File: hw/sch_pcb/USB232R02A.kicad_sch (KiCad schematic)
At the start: 36 parts, among them J1 USB_B, J10 HEADER_2x01_PARALLEL, J11 HEADER_2x01_PARALLEL, J12 HEADER_2x01_PARALLEL, J13 HEADER_2x01_PARALLEL, J14 HEADER_2x01_PARALLEL, J15 HEADER_2x01_PARALLEL, J16 HEADER_2x01_PARALLEL, J2 HEADER_2x03_PARALLEL, J3 HEADER_2x03_PARALLEL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

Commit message: Edit
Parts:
- removed J13, J14, J15, J16: HEADER_2x01_PARALLEL, Mlab_Pin_Headers:Straight_2x01, symbol MLAB_HEADER:HEADER_2x01_PARALLEL
- added F1: 750mA, Mlab_F:1812, symbol Device:Polyfuse
- added J13, J14, J15, J16: -, Mlab_Pin_Headers:Straight_1x01, symbol MLAB_HEADER:HEADER_1x01
- added J17: HEADER_2x01_PARALLEL, Mlab_Pin_Headers:Straight_2x01, symbol MLAB_HEADER:HEADER_2x01_PARALLEL
- H1, H2, H3, H4: footprint Mlab_Mechanical:dira_3mm -> Mlab_Mechanical:MountingHole_3mm
- J10, J11, J12, J4, J9: value HEADER_2x01_PARALLEL -> -
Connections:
- net CBUS0: now also J13.1
- net CBUS3: now also J16.1
- net D+: now also U1.4 (I/O2); no longer U1.6 (I/O1)
- net D-: now also U1.6 (I/O1); no longer U1.4 (I/O2)
- net DM: now also U1.1 (I/O1); no longer U1.3 (I/O2)
- net DP: now also U1.3 (I/O2); no longer U1.1 (I/O1)
- net GND: now also J17.1, J17.2
- net RXLED/CBUS1: now also J14.1
- net TXLED/CBUS2: now also J15.1
- net VBUS: now also F1.1; no longer C1.1, FB1.1
- new net: C1.1, F1.2, FB1.1

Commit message: Add MLAB title block. Minor layout cleanup Cleanup silkscreen.
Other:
- company: (none) -> jacho
- title: (none) -> USB232R02A

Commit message: Edit
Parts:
- C1: UST_ID (none) -> 5c70984712875079b91f8b49
- C2: UST_ID (none) -> 5c70984812875079b91f8bbd
- C3, C4, C5: UST_ID (none) -> 5c70984712875079b91f8b4c
- D1: UST_ID (none) -> 5c70984512875079b91f88ac
- D2: UST_ID (none) -> 5c70984412875079b91f8896
- D3: UST_ID (none) -> 5c70984412875079b91f8895
- F1: UST_ID (none) -> 5c70984512875079b91f88d2
- J1: UST_ID (none) -> 5c70984412875079b91f87a8
- R1: UST_ID (none) -> 5c70984612875079b91f8995
- R2: UST_ID (none) -> 5c70984612875079b91f899f
- R3, R4: UST_ID (none) -> 5c70984512875079b91f8983
- U1: UST_ID (none) -> 5e82e0691287502a334a778c
- U2: UST_ID (none) -> 605d7fe0128750769e769adb

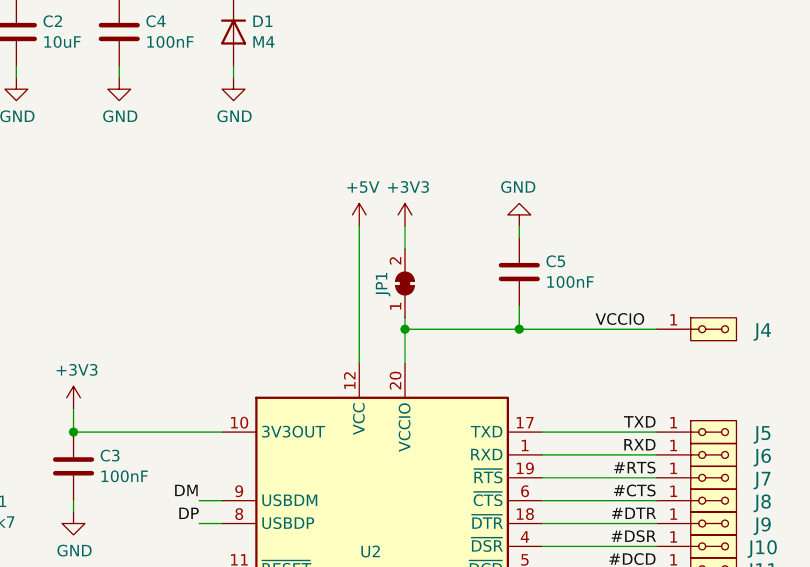
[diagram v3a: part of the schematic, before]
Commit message: vyreseni DRC, uprava sablon
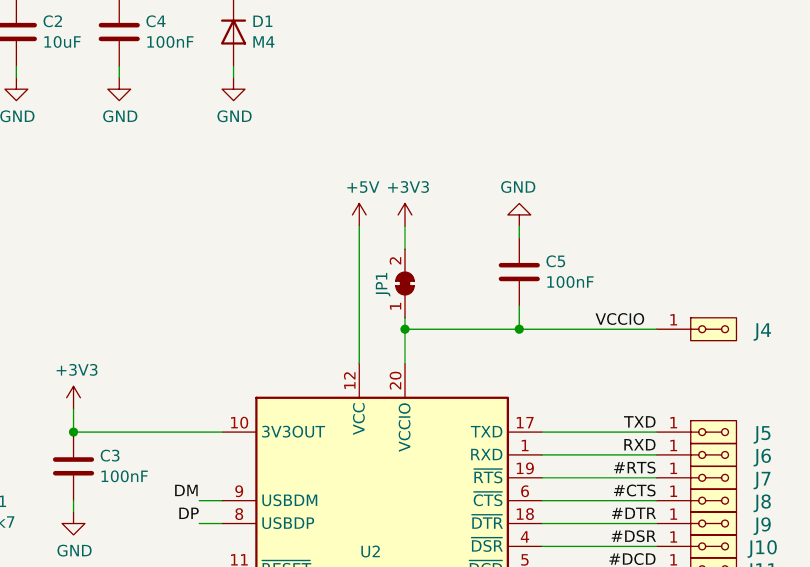
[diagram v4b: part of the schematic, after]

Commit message: Update title block and resolve ERC issues.
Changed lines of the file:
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@@
     (date "2021-03-25")
     (company "jacho")
+    (comment 1 "USB to UART converter")
   )
   (junction (at 54.61 30.48) (diameter 1.016) (color 0 0 0 0)
@@
     (stroke (width 0) (type solid) (color 0 0 0 0))
   )
+  (wire (pts (xy 152.4 93.98) (xy 152.4 95.25))
+    (stroke (width 0) (type default) (color 0 0 0 0))
+  )
   (wire (pts (xy 96.52 55.88) (xy 96.52 57.15))
     (stroke (width 0) (type solid) (color 0 0 0 0))
@@
   (wire (pts (xy 91.44 55.88) (xy 91.44 110.49))
     (stroke (width 0) (type solid) (color 0 0 0 0))
+  )
+  (wire (pts (xy 120.65 55.88) (xy 125.095 55.88))
+    (stroke (width 0) (type default) (color 0 0 0 0))
   )
   (wire (pts (xy 77.47 64.77) (xy 77.47 66.04))
@@
   (label "D+" (at 41.91 27.94 180)
     (effects (font (size 1.27 1.27)) (justify right bottom))
+  )
+  (symbol (lib_id "power:PWR_FLAG") (at 152.4 95.25 180) (unit 1)
+    (in_bom yes) (on_board yes) (fields_autoplaced)
+    (property "Reference" "#FLG0102" (id 0) (at 152.4 97.155 0)
+      (effects (font (size 1.27 1.27)) hide)
+    )
+    (property "Value" "PWR_FLAG" (id 1) (at 152.4 99.6934 0))
+    (property "Footprint" "" (id 2) (at 152.4 95.25 0)
+      (effects (font (size 1.27 1.27)) hide)
+    )
+    (property "Datasheet" "~" (id 3) (at 152.4 95.25 0)
+      (effects (font (size 1.27 1.27)) hide)
+    )
+    (pin "1")
   )
   (symbol (lib_id "Device:LED") (at 226.06 133.35 90) (unit 1)
@@
     (pin "1")
   )
+  (symbol (lib_id "power:PWR_FLAG") (at 125.095 55.88 270) (unit 1)
+    (in_bom yes) (on_board yes) (fields_autoplaced)
+    (property "Reference" "#FLG0101" (id 0) (at 127 55.88 0)
+      (effects (font (size 1.27 1.27)) hide)
+    )
+    (property "Value" "PWR_FLAG" (id 1) (at 128.27 56.3138 90)
+      (effects (font (size 1.27 1.27)) (justify left))
+    )
+    (property "Footprint" "" (id 2) (at 125.095 55.88 0)
+      (effects (font (size 1.27 1.27)) hide)
+    )
+    (property "Datasheet" "~" (id 3) (at 125.095 55.88 0)
+      (effects (font (size 1.27 1.27)) hide)
+    )
+    (pin "1")
+  )
   (symbol (lib_id "Device:R") (at 91.44 127 0) (unit 1)
     (in_bom yes) (on_board yes)
@@
   )
   (symbol_instances
+    (path "/a44fa378-8070-49fe-8648-d05e4acc2bf6"
+      (reference "#FLG0101") (unit 1) (value "PWR_FLAG") (footprint "")
+    )
+    (path "/04280950-d8b5-4e58-a843-833a62f58e66"
+      (reference "#FLG0102") (unit 1) (value "PWR_FLAG") (footprint "")
+    )
     (path "/e9f2670e-53e6-4529-93e0-64ee9fdad578"
       (reference "#PWR0101") (unit 1) (value "GND") (footprint "")
